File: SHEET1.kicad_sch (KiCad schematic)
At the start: 26 parts, among them U10 74LS373, U11 8284A, U2 8259A, U3 8088, U4 8087 SOCKET, U6 8288, U7 74LS373, U8 74LS245, U84 74LS10, U9 74LS373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

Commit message: Fixed LS and S parts
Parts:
- U84: value 74LS10 -> 74S10
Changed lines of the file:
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@@
 			)
 		)
-		(property "Value" "74LS10"
+		(property "Value" "74S10"
 			(at 353.06 210.82 0)
 			(effects

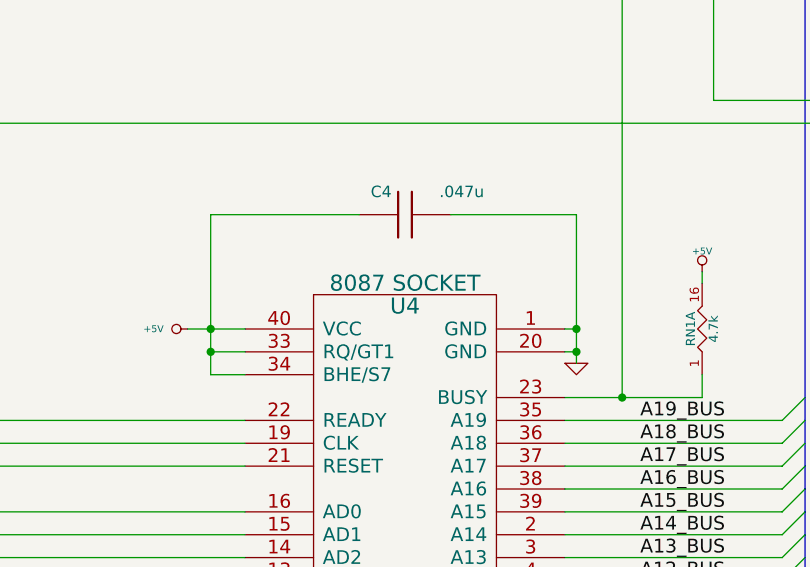
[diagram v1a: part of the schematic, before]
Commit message: added BOM
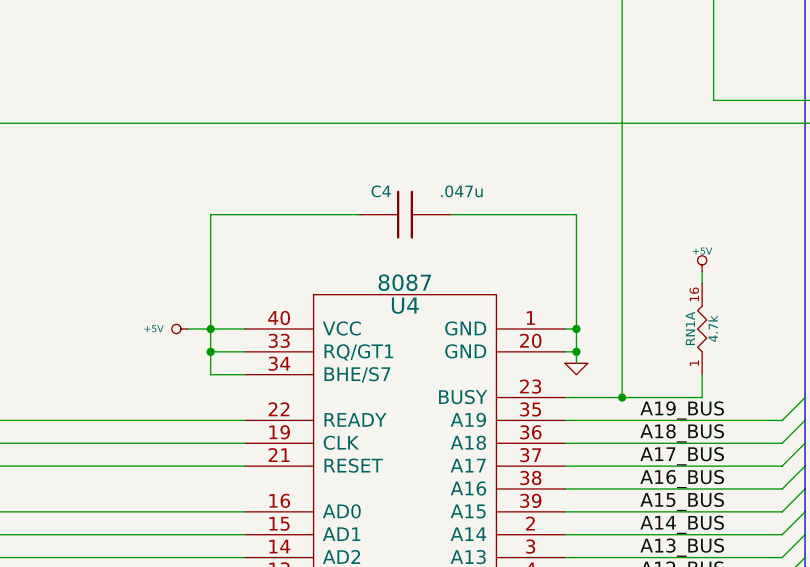
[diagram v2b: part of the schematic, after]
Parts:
- C16, C4: Link (none) -> https://www.digikey.com/en/products/detail/vishay-beyschlag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; Note (none) -> No reason not to use 100n here
- R13, R14, R15, R16, R17, R18, R19, R21: Link (none) -> https://www.digikey.com/en/products/detail/yageo/MFR-25FTE5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
- R22, R25: Link (none) -> https://www.digikey.com/en/products/detail/yageo/MFR-25FBF5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
- RN1, RN3: Link (none) -> https://www.digikey.com/en/products/detail/bourns-inc/4116R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
- U10, U7, U8, U9: Link (none) -> https://www.digikey.com/en/products/detail/texas-instrument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
- U11: Link (none) -> https://www.questcomp.com/part/4/cp82c84a/146639293
- U2: Link (none) -> https://www.jameco.com/z/P8259A-Intel-Corporation-IC-8259-P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
- U3: Link (none) -> https://www.jameco.com/z/P8088-2-Advanced-Micro-Devices-MPU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
- U4: value 8087 SOCKET -> 8087; Link (none) -> https://www.questcomp.com/part/4/c8087/126791059
- U6: Link (none) -> https://www.questcomp.com/part/4/cp82c88/146639310
- U84: Link (none) -> https://www.mouser.com/ProductDetail/Texas-Instruments/SN74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
- VC1: Link (none) -> https://www.digikey.com/en/products/detail/ew-electronics/G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; Note (none) -> Bend the leads a bit to fit across pins 1 and 2.
- Y1: Link (none) -> https://www.digikey.com/en/products/detail/cts-frequency-co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
